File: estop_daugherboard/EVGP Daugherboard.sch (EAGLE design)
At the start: 36 parts, among them J1 E-STOP HEADER, J2 AVR_SPI_PROG_3X2PTH, J3 UX60-MB-5S8, J4 B4B-XH-A(LF)(SN), U1 ATMEGA32U4-AU, U4 NL27WZ08USG, X1 TSX-3225 16.0000MF18X-AC0

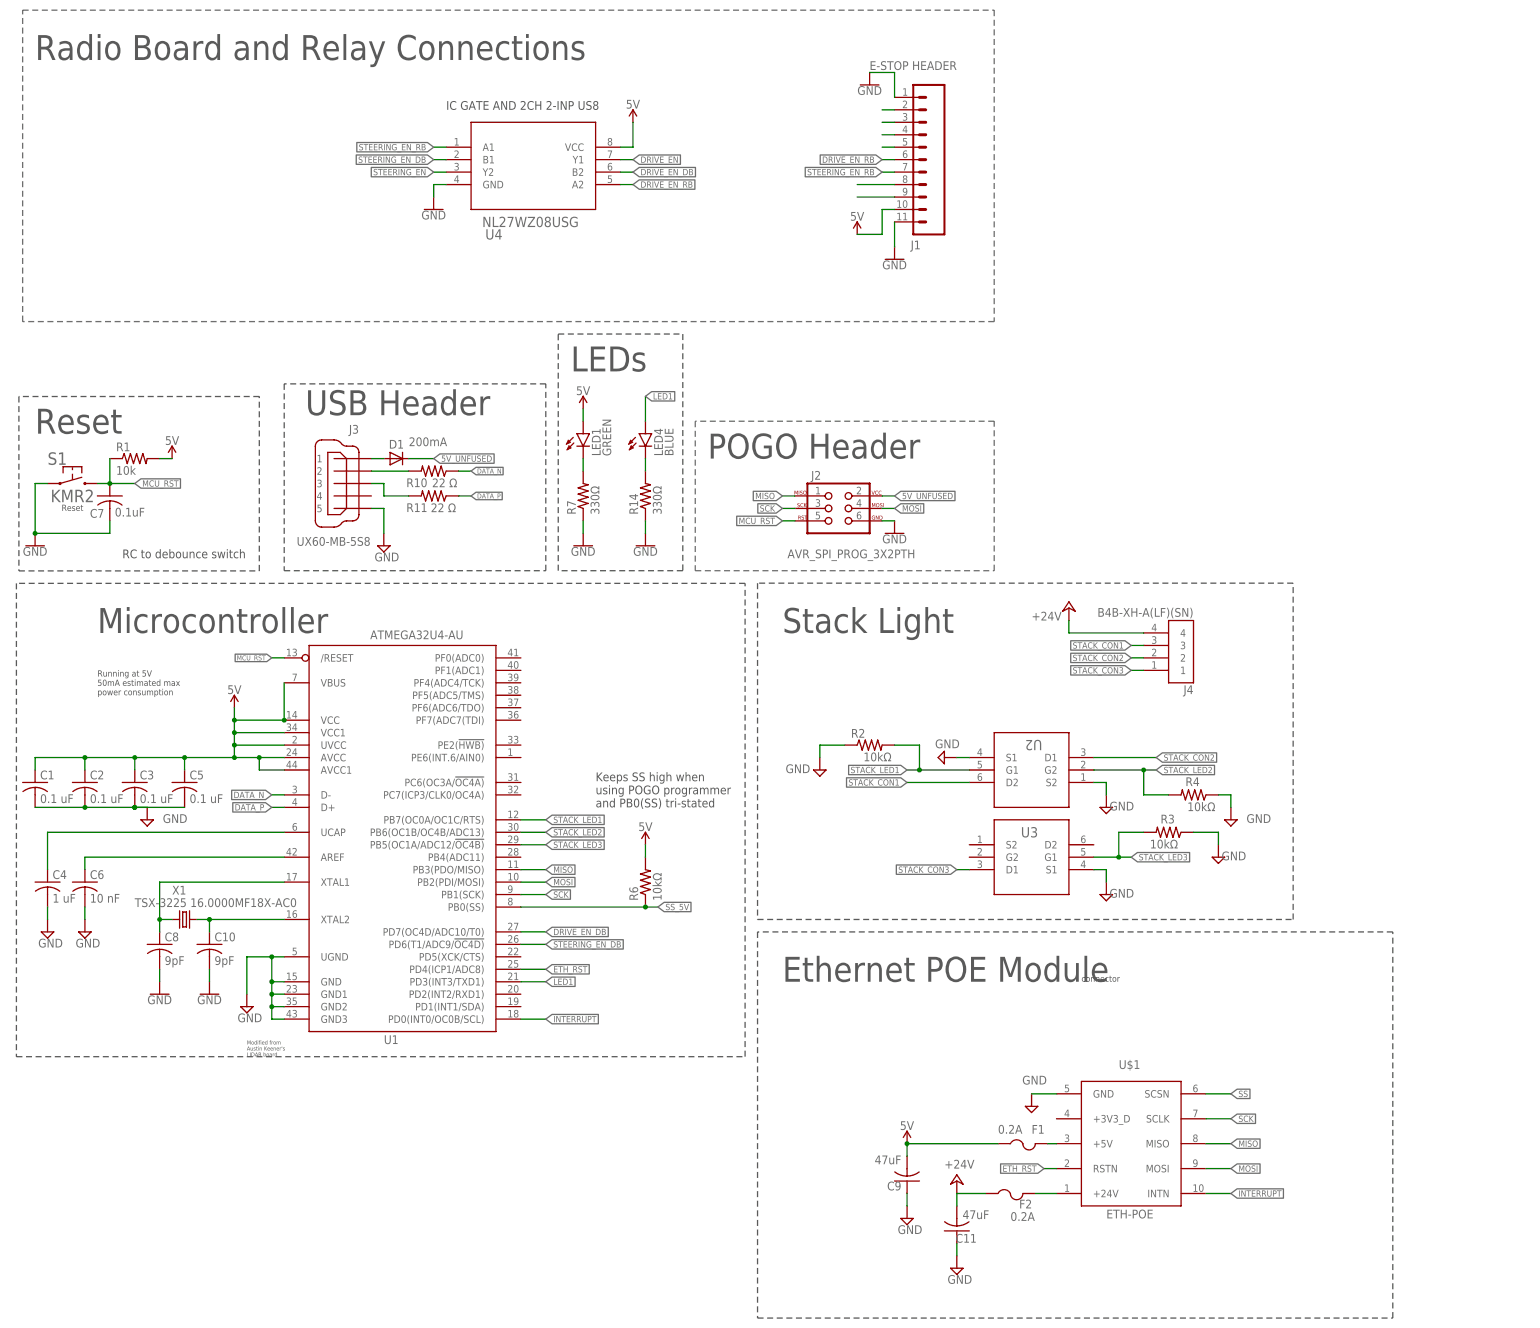
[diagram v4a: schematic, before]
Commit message: schematic updates, connectors
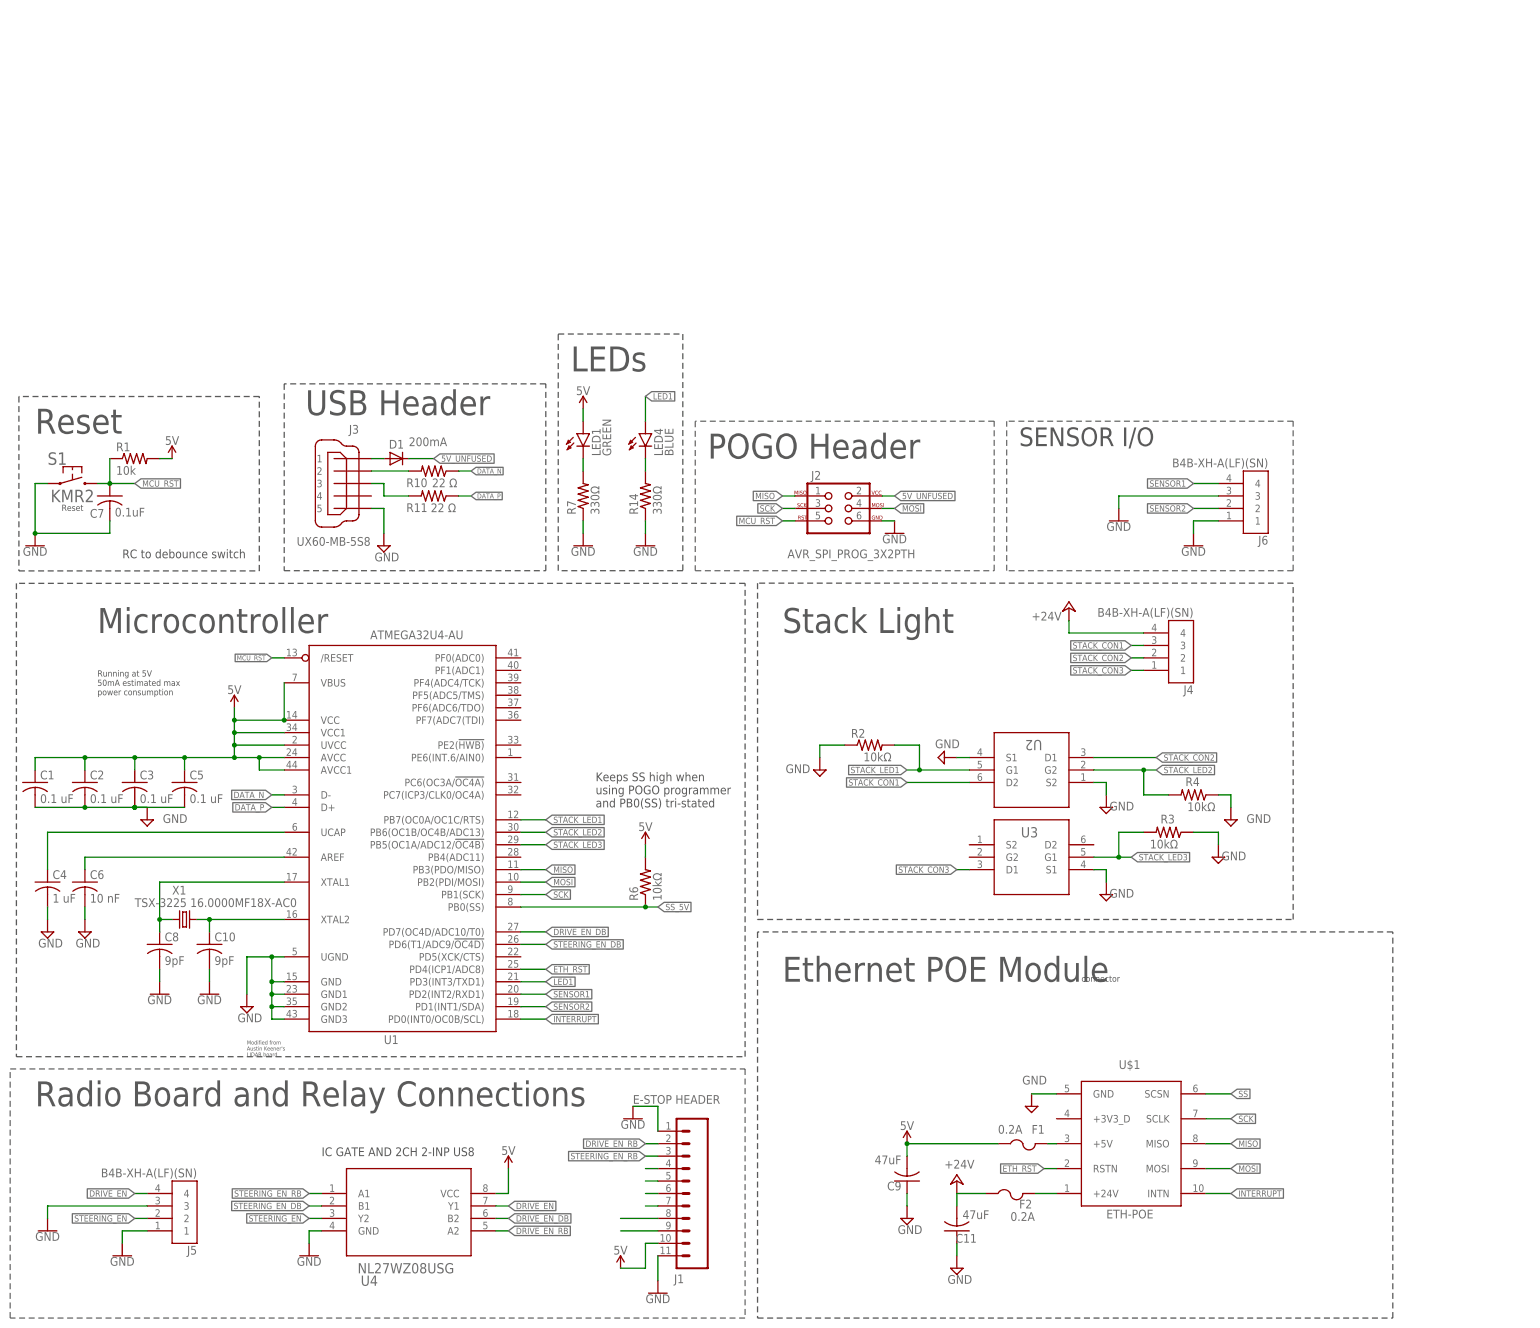
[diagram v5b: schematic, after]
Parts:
- added J5, J6: B4B-XH-A(LF)(SN), JST-XH-Connector:B4B-XH-A(LF)(SN)
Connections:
- removed net DIO_1: J1.3
- removed net MCU_RST1: J1.2
- new net N$1: J1.6
- new net N$8: J1.7
- new net SENSOR1: J6.4, U1.PD2(INT2/RXD1)
- new net SENSOR2: J6.2, U1.PD1(INT1/SDA)
- net DRIVE_EN: now also J5.4
- net DRIVE_EN_RB: now also J1.2; no longer J1.6
- net GND: now also J5.1, J5.3, J6.1, J6.3
- net STEERING_EN: now also J5.2
- net STEERING_EN_RB: now also J1.3; no longer J1.7
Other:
- note added: "SENSOR I/O"
- moved on the sheet: J1, U4

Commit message: Changed 4-pin JST library and some other small stuff
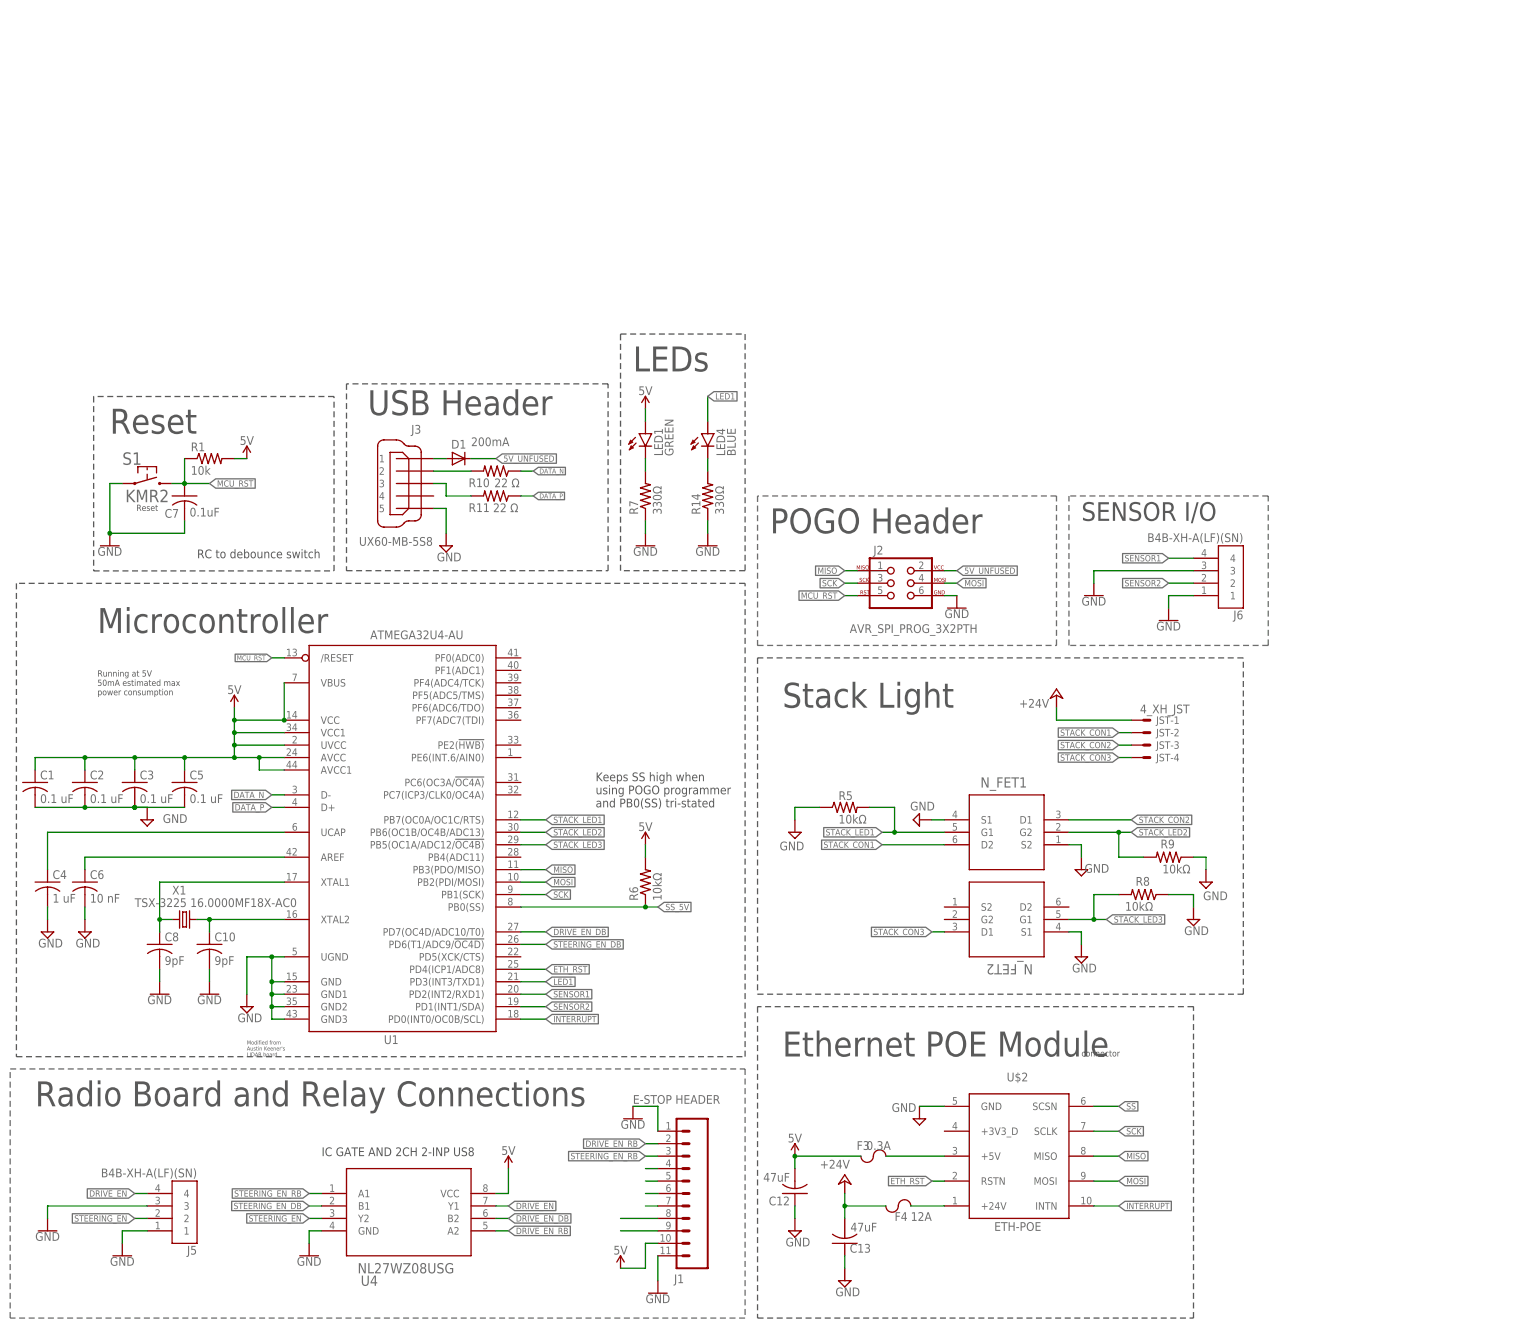
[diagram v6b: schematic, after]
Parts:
- removed C11, C9: 47uF, resistor:C-USC0603
- removed F1, F2: 0.2A, adafruit:PTCFUSE-1206
- removed J4: B4B-XH-A(LF)(SN), JST-XH-Connector:B4B-XH-A(LF)(SN)
- removed R2, R3, R4: 10kΩ, rcl:R-US_R0603
- removed U$1: ETH-POE, ethernet_poe:ETH-POE
- removed U2, U3: (no value), DownloadedParts:BSS84DW-7-F
- added C12, C13: 47uF, resistor:C-USC0603
- added F3: 0.3A, RoboJackets-Fuses:CHIP_FUSE1206
- added F4: 12A, RoboJackets-Fuses:CHIP_FUSE1206
- added JST: 4_XH_JST, Rembrandt Electronics - JST XH Connectors v1-0:JST-XH-04-PIN-LONG-PAD
- added R5, R8, R9: 10kΩ, rcl:R-US_R0603
- added U$2: ETH-POE, ethernet_poe:ETH-POE
- added U5: N_FET1, DownloadedParts:BSS84DW-7-F
- added U6: N_FET2, DownloadedParts:BSS84DW-7-F
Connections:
- removed net N$2: F1.2, U$1.+5V
- removed net N$4: F2.2, U$1.+24V
- new net N$10: F3.2, U$2.+5V
- new net N$9: F4.2, U$2.+24V
- net +24V: now also C13.2, F4.1, JST-1.S; no longer C11.2, F2.1, J4.4
- net 5V: now also C12.2, F3.1; no longer C9.2, F1.1
- net ETH_RST: now also U$2.RSTN; no longer U$1.RSTN
- net GND: now also C12.1, C13.1, R5.1, R8.1, R9.1, U$2.GND, U5.S1, U5.S2, U6.S1; no longer C11.1, C9.1, R2.1, R3.1, R4.1, U$1.GND, U2.S1, U2.S2, U3.S1
- net INTERRUPT: now also U$2.INTN; no longer U$1.INTN
- net MISO: now also U$2.MISO; no longer U$1.MISO
- net MOSI: now also U$2.MOSI; no longer U$1.MOSI
- net SCK: now also U$2.SCLK; no longer U$1.SCLK
- net SS: now also U$2.SCSN; no longer U$1.SCSN
- net STACK_CON1: now also JST-2.S, U5.D2; no longer J4.3, U2.D2
- net STACK_CON2: now also JST-3.S, U5.D1; no longer J4.2, U2.D1
- net STACK_CON3: now also JST-4.S, U6.D1; no longer J4.1, U3.D1
- net STACK_LED1: now also R5.2, U5.G1; no longer R2.2, U2.G1
- net STACK_LED2: now also R9.2, U5.G2; no longer R4.2, U2.G2
- net STACK_LED3: now also R8.2, U6.G1; no longer R3.2, U3.G1
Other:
- moved on the sheet: C7, D1, J2, J3, J6, LED1, LED4, R1, R10, R11, R14, R7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

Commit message: schematic updates, connectors changes
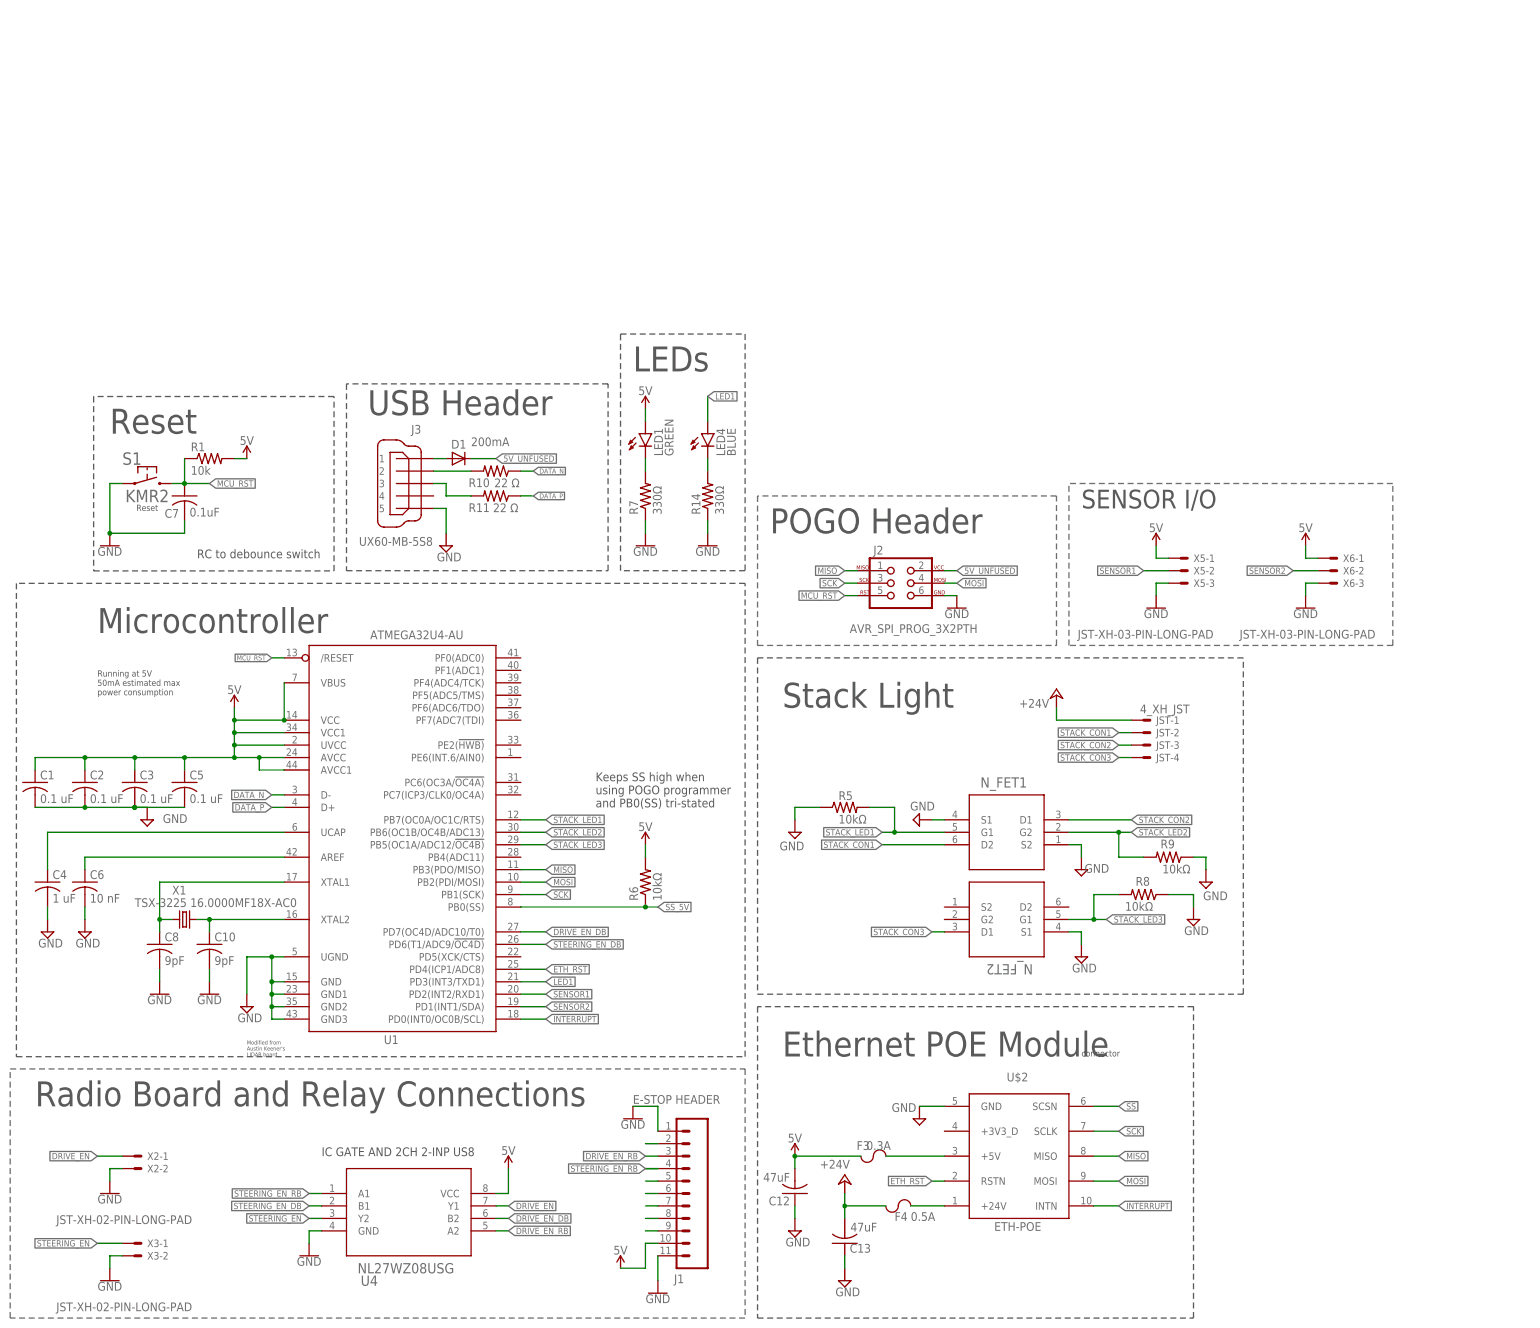
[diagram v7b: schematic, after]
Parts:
- removed J5, J6: B4B-XH-A(LF)(SN), JST-XH-Connector:B4B-XH-A(LF)(SN)
- added X2, X3: JST-XH-02-PIN-LONG-PAD, Rembrandt Electronics - JST XH Connectors v1-0:JST-XH-02-PIN-LONG-PAD
- added X5, X6: JST-XH-03-PIN-LONG-PAD, Rembrandt Electronics - JST XH Connectors v1-0:JST-XH-03-PIN-LONG-PAD
- F4: value 12A -> 0.5A
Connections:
- net DIO_6_R renamed N$4
- net DIO_7_R renamed N$12
- new net N$2: J1.2
- net 5V: now also X5-1.S, X6-1.S
- net DRIVE_EN: now also X2-1.S; no longer J5.4
- net DRIVE_EN_RB: now also J1.3; no longer J1.2
- net GND: now also X2-2.S, X3-2.S, X5-3.S, X6-3.S; no longer J5.1, J5.3, J6.1, J6.3
- net SENSOR1: now also X5-2.S; no longer J6.4
- net SENSOR2: now also X6-2.S; no longer J6.2
- net STEERING_EN: now also X3-1.S; no longer J5.2
- net STEERING_EN_RB: no longer J1.3

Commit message: Started work on routing
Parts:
- C12: device resistor:C-USC0603 -> rcl:C-USC1206K
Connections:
- removed net N$10: F3.2, U$2.+5V
- removed net STACK_LED1: R5.2, U1.PB7(OC0A/OC1C/RTS), U5.G1
- removed net STACK_LED2: R9.2, U1.PB6(OC1B/OC4B/ADC13), U5.G2
- removed net STACK_LED3: R8.2, U1.PB5(OC1A/ADC12/!OC4B), U6.G1
- new net DRIVE_E_DB: U1.PF1(ADC1)
- new net STACK_MCU1: R5.2, U1.PF5(ADC5/TMS), U5.G1
- new net STACK_MCU2: R9.2, U1.PF6(ADC6/TDO), U5.G2
- new net STACK_MCU3: R8.2, U1.PF7(ADC7(TDI), U6.G1
- net 5V_UNFUSED: now also F3.2, U$2.+5V
- net DRIVE_EN_DB: no longer U1.PD7(OC4D/ADC10/T0)
- net ETH_RST: now also U1.PC7(ICP3/CLK0/OC4A); no longer U1.PD4(ICP1/ADC8)
- net INTERRUPT: now also U1.PE2(!HWB); no longer U1.PD0(INT0/OC0B/SCL)
- net SENSOR1: now also U1.PD6(T1/ADC9/!OC4D); no longer U1.PD2(INT2/RXD1)
- net SENSOR2: now also U1.PD4(ICP1/ADC8); no longer U1.PD1(INT1/SDA)
- net SS: now also U1.PC6(OC3A/!OC4A)
- net STEERING_EN_DB: now also U1.PF0(ADC0); no longer U1.PD6(T1/ADC9/!OC4D)
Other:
- moved on the sheet: C12, F3
